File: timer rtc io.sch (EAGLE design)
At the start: 71 parts, among them T1 BC547, U1 74HC245, U10 74HC688, U11 74LS30N, U12 74LS00N, U13 74HC32, U14 74HC04, U15 74HC08, U16 74HC688, U17 74HC138, U18 74HC138, U19 74HC573, U2 74HC245, U20 74HC573, U21 74HC573, U22 74HC573, U23 74HC573, U3 74HC245, U4 74HC688, U6 74HC74, U7 74HC590, U8 74HC688, U9 BQ4845, X1 32.768KHz, Y1 4.096MHz

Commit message: A few changes:
* renamed source files to .s
* moved some stuff to .inc files
* a couple of HW updates to some boars to provide a bigger RAM space for UART loading
* SIO module for serial comms
* serial loader code to work with the above
* scripts for loading/reading/executing via serial

I think thats it...
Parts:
- added C26, C27, C28: 100nF, rcl:C-EU050-025X075
- added R3: 10K, rcl:R-EU_0207/10
- added R4, R5: 560R, rcl:R-EU_0207/10
- added U24: NE555, st-microelectronics:NE555
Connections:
- removed net N$48: U11A.I6, U17A.Y3, U22A.C, U22A.OC
- new net N$53: BUS-15.S, R3.1, U5.IEI
- new net N$60: R1.1, SG1.2, U24.OUT
- new net N$88: R4.1, R5.2, U24.DIS
- new net N$89: C28.1, R5.1, U24.TRE, U24.TRI
- new net N$90: U11A.I6, U17A.Y3, U21A.C, U21A.OC
- net +5V: now also C26.1, R3.2, R4.2, U24.VCC+; no longer U5.IEI
- net GND: now also C26.2, C27.2, C28.2, U24.GND
- net N$47: now also U22A.C, U22A.OC; no longer U21A.C, U21A.OC
- net N$55: now also C27.1, U24.CON; no longer R2.1, U23A.8Q
- net N$56: now also U23A.8Q, U24./RES; no longer R1.1, SG1.2, T1.C
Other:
- note added: "BUTTONS 08"
- note added: "OUTPUTS 0C"
- note added: "R4=560R R5=560R ~66% D/C ~8.6KHZ R4=1K5 R5=150R ~91% D/C ~8KHZ"
- note added: "SWITCHES 1 09"
- note added: "SWITCHES 2 0A"
- note added: "SWITCHES 3 0B"
- moved on the sheet: BUS-15, C10, C11, C12, C13, C14, C15, C16, C17, C18, C19, C2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

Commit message: Discovered issue with Timer/RTC/IO board
The original design of the Timer/RTC/IO board did not cater for a situation where multiple Z80 peripherals may exist in the system.

Consequently, when M1/ and IORQ/ are both asserted by the CPU to read a vector from the interrupting peripheral, and if that peripheral happens to be the SIO, the Timer/RTC/IO board will configure its data bus buffer for output towards the CPU. If the SIO is responding with its vector, this causes contention on that portion of the bus, resulting in interupts to random vectors.

Staged some logic for a subsequent modification (gates U14B and U13A) which would prevent the Timer/RTC/IO board from configuring its data bus buffer outwards if the IEI/ signal is asserted. However, this logic isnt latched in any way, so it could be interrupted half way through if IEI/ is asserted while outputting a vector... Perhaps more thought needed.
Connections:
- new net !IEI!: BUS-15.S, R3.1, U14B.I, U5.IEI
- new net N$48: U13A.O
- net GND: no longer U13A.I0, U13A.I1, U14B.I
- net N$53: now also U13A.I0, U14B.O; no longer BUS-15.S, R3.1, U5.IEI
- net N$61: now also U13A.I1
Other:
- moved on the sheet: BAT1, BUS-15, JP1, R3, RN2-1, RN2-2, RN2-3, RN2-4, RN2_, U10, U13A, U14A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

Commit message: Interrupt daisy chain modification
To overcome the issue identified earlier, it seems better to change the interrupt daisy chain to make the CTC the higher priority device. This also simplifies the extra required circuitry to only a single OR gate (U13A).

Now, only when the IEO/ signal of the CTC is asserted will the board drive the data bus to the CPU.

Also added in a previous revision is changes to the beeper circuit. Will now be driven by a 555 timer, gated by the output register.
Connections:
- removed net !IEI!: BUS-15.S, R3.1, U14B.I, U5.IEI
- removed net N$53: U13A.I0, U14B.O
- new net !IEO!: BUS-15.S, U13A.I0, U5.IEO
- net +5V: now also U5.IEI; no longer R3.2
- net GND: now also U14B.I
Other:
- moved on the sheet: BUS-15, R3, U11, U12A, U13A, U13C, U14B, U14F, U15A

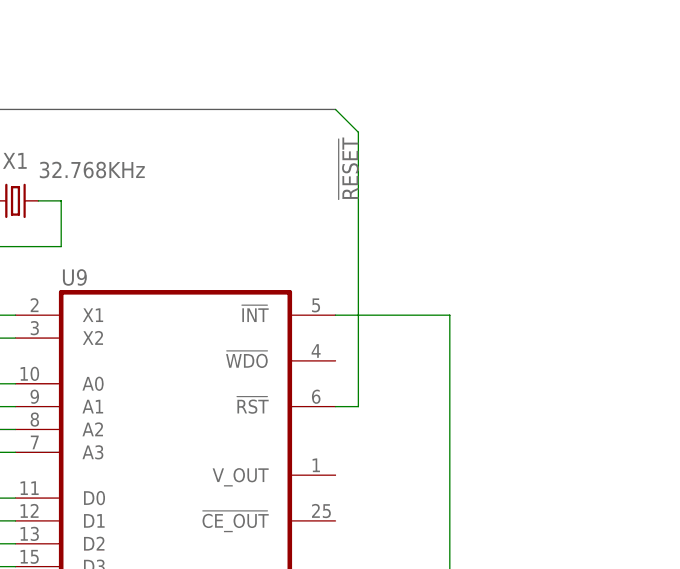
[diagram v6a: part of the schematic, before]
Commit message: Add jumper to output of RST/ pin on RTC
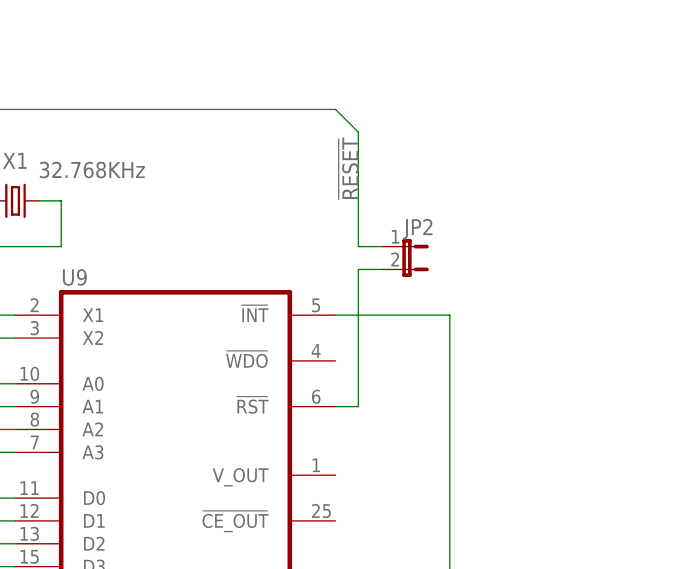
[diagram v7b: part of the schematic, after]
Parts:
- added JP2: (no value), jumper:JP1E
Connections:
- new net N$53: JP2.2, U9.!RST!
- net !RESET!: now also JP2.1; no longer U9.!RST!
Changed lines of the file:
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@@
 <part name="C28" library="rcl" deviceset="C-EU" device="050-025X075" value="100nF"/>
 <part name="GND32" library="supply1" deviceset="GND" device=""/>
+<part name="JP2" library="jumper" deviceset="JP1E" device=""/>
 </parts>
 <sheets>
@@
 <attribute name="VALUE" x="228.6" y="-127" size="1.778" layer="96"/>
 </instance>
+<instance part="JP2" gate="A" x="535.94" y="147.32" smashed="yes" rot="R270">
+<attribute name="NAME" x="535.94" y="148.59" size="1.778" layer="95"/>
+<attribute name="VALUE" x="535.94" y="141.605" size="1.778" layer="96"/>
+</instance>
 </instances>
 <busses>
@@
 <segment>
 <wire x1="528.32" y1="162.56" x2="530.86" y2="160.02" width="0.1524" layer="91"/>
-<wire x1="530.86" y1="160.02" x2="530.86" y2="129.54" width="0.1524" layer="91"/>
-<pinref part="U9" gate="G$1" pin="!RST!"/>
-<wire x1="530.86" y1="129.54" x2="528.32" y2="129.54" width="0.1524" layer="91"/>
+<wire x1="530.86" y1="160.02" x2="530.86" y2="147.32" width="0.1524" layer="91"/>
+<pinref part="JP2" gate="A" pin="1"/>
+<wire x1="533.4" y1="147.32" x2="530.86" y2="147.32" width="0.1524" layer="91"/>
 <label x="530.86" y="152.4" size="1.778" layer="95" rot="R90"/>
 </segment>
@@
 </segment>
 </net>
+<net name="N$53" class="0">
+<segment>
+<pinref part="U9" gate="G$1" pin="!RST!"/>
+<wire x1="530.86" y1="144.78" x2="530.86" y2="129.54" width="0.1524" layer="91"/>
+<wire x1="530.86" y1="129.54" x2="528.32" y2="129.54" width="0.1524" layer="91"/>
+<pinref part="JP2" gate="A" pin="2"/>
+<wire x1="533.4" y1="144.78" x2="530.86" y2="144.78" width="0.1524" layer="91"/>
+</segment>
+</net>

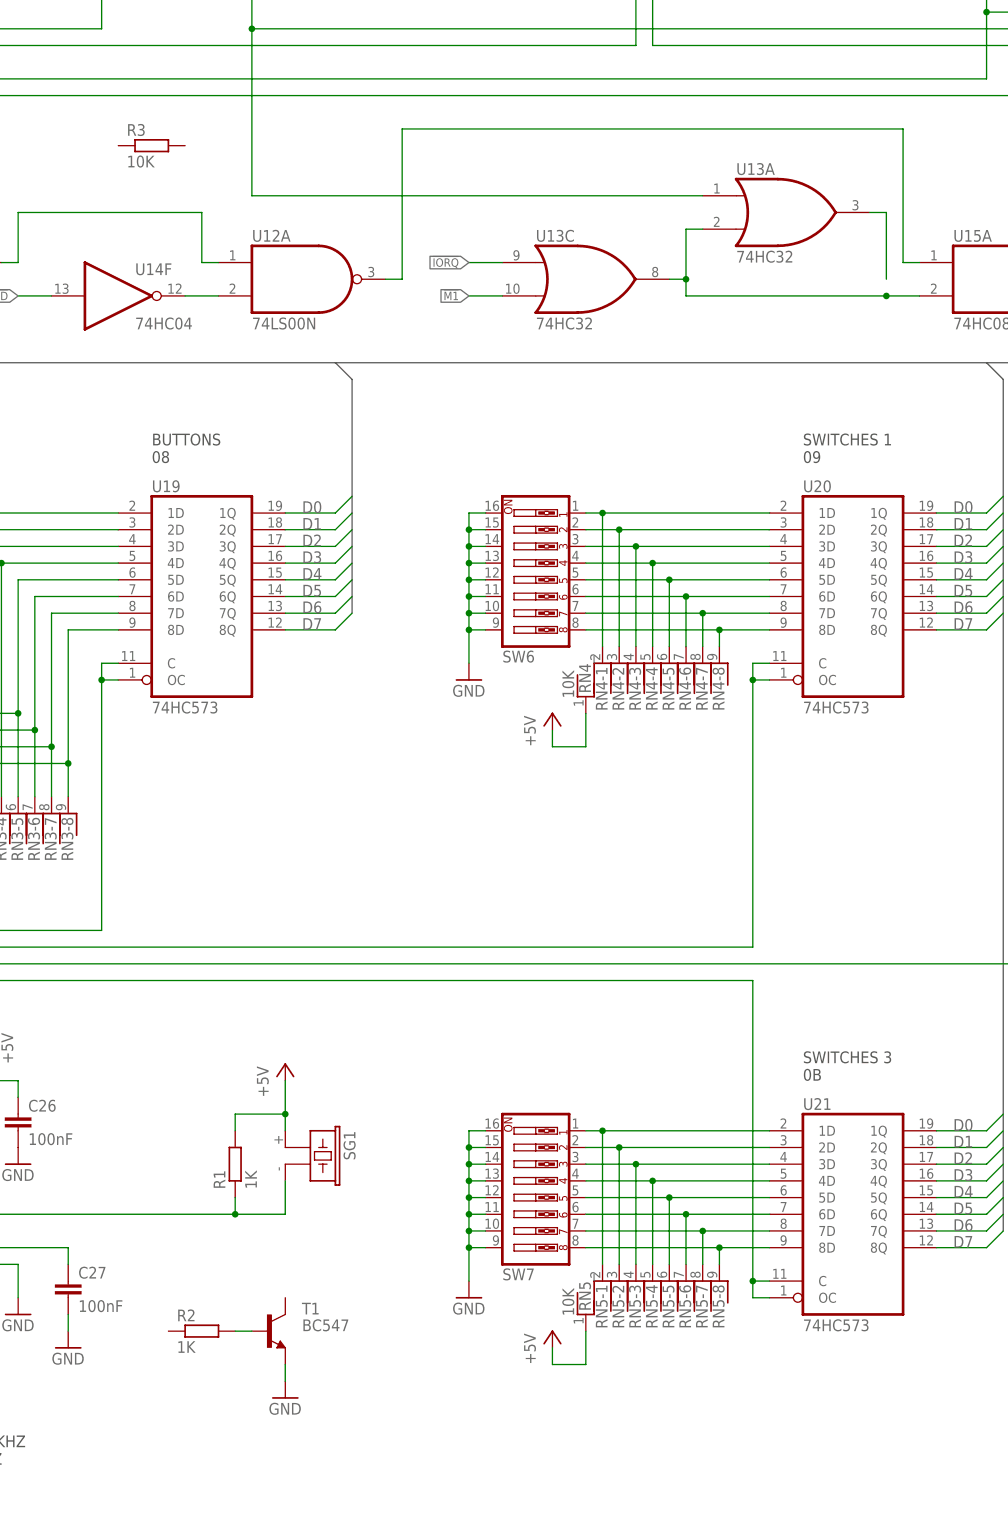
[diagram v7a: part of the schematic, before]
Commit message: Correct schematic for new interrupt daisy chain priority
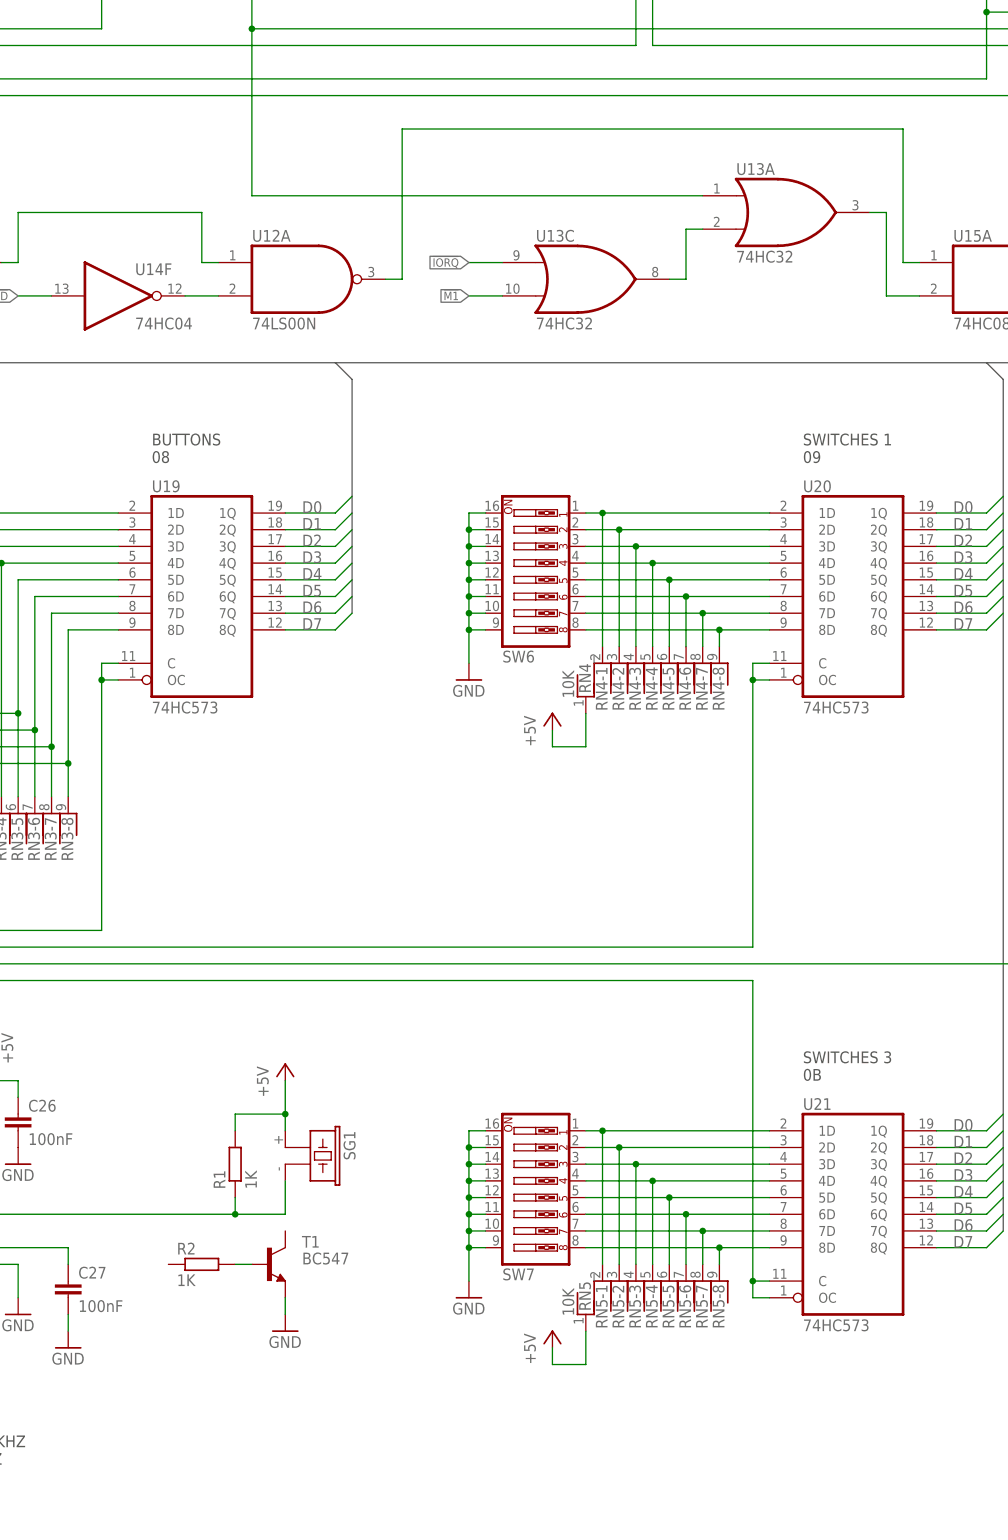
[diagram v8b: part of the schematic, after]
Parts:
- removed R3: 10K, rcl:R-EU_0207/10
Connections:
- removed net N$61: U13A.I1, U13C.O, U15A.I1
- new net N$91: U13A.I1, U13C.O
- net N$48: now also U15A.I1
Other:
- moved on the sheet: R2, T1
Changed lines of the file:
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@@
 <part name="GND28" library="supply1" deviceset="GND" device=""/>
 <part name="C25" library="rcl" deviceset="C-EU" device="050-025X075" value="100nF"/>
-<part name="R3" library="rcl" deviceset="R-EU_" device="0207/10" value="10K"/>
 <part name="U24" library="st-microelectronics" deviceset="NE555" device=""/>
 <part name="P+23" library="supply1" deviceset="+5V" device=""/>
@@
 <text x="195.58" y="-76.2" size="1.778" layer="97">OUTPUTS
 0C</text>
-<wire x1="223.52" y1="-68.58" x2="327.66" y2="-68.58" width="0.6096" layer="90"/>
-<wire x1="327.66" y1="-68.58" x2="327.66" y2="-144.78" width="0.6096" layer="90"/>
+<wire x1="223.52" y1="-71.12" x2="327.66" y2="-71.12" width="0.6096" layer="90"/>
+<wire x1="327.66" y1="-71.12" x2="327.66" y2="-144.78" width="0.6096" layer="90"/>
 <wire x1="327.66" y1="-144.78" x2="223.52" y2="-144.78" width="0.6096" layer="90"/>
-<wire x1="223.52" y1="-144.78" x2="223.52" y2="-68.58" width="0.6096" layer="90"/>
+<wire x1="223.52" y1="-144.78" x2="223.52" y2="-71.12" width="0.6096" layer="90"/>
 <text x="228.6" y="-139.7" size="1.778" layer="97">R4=560R R5=560R ~66% D/C ~8.6KHZ
 R4=1K5 R5=150R ~91% D/C ~8KHZ</text>
-<wire x1="363.22" y1="63.5" x2="447.04" y2="63.5" width="0.6096" layer="90"/>
-<wire x1="447.04" y1="63.5" x2="447.04" y2="33.02" width="0.6096" layer="90"/>
-<wire x1="447.04" y1="33.02" x2="363.22" y2="33.02" width="0.6096" layer="90"/>
-<wire x1="363.22" y1="33.02" x2="363.22" y2="63.5" width="0.6096" layer="90"/>
 </plain>
 <instances>
@@
 <attribute name="VALUE" x="314.96" y="-97.79" size="1.778" layer="96" rot="R270"/>
 </instance>
-<instance part="GND17" gate="1" x="312.42" y="-129.54" smashed="yes">
-<attribute name="VALUE" x="309.88" y="-132.08" size="1.778" layer="96"/>
+<instance part="GND17" gate="1" x="312.42" y="-119.38" smashed="yes">
+<attribute name="VALUE" x="309.88" y="-121.92" size="1.778" layer="96"/>
 </instance>
 <instance part="P+13" gate="1" x="312.42" y="-78.74" smashed="yes">
@@
 <attribute name="VALUE" x="27.94" y="-60.96" size="1.778" layer="96"/>
 </instance>
-<instance part="T1" gate="G$1" x="309.88" y="-119.38" smashed="yes">
-<attribute name="NAME" x="314.96" y="-116.84" size="1.778" layer="95"/>
-<attribute name="VALUE" x="314.96" y="-119.38" size="1.778" layer="96"/>
-</instance>
-<instance part="R2" gate="G$1" x="299.72" y="-119.38" smashed="yes">
-<attribute name="NAME" x="295.91" y="-117.8814" size="1.778" layer="95"/>
-<attribute name="VALUE" x="295.91" y="-122.682" size="1.778" layer="96"/>
+<instance part="T1" gate="G$1" x="309.88" y="-109.22" smashed="yes">
+<attribute name="NAME" x="314.96" y="-106.68" size="1.778" layer="95"/>
+<attribute name="VALUE" x="314.96" y="-109.22" size="1.778" layer="96"/>
+</instance>
+<instance part="R2" gate="G$1" x="299.72" y="-109.22" smashed="yes">
+<attribute name="NAME" x="295.91" y="-107.7214" size="1.778" layer="95"/>
+<attribute name="VALUE" x="295.91" y="-112.522" size="1.778" layer="96"/>
 </instance>
 <instance part="U11" gate="A" x="256.54" y="43.18" smashed="yes">
@@
 <attribute name="VALUE" x="481.584" y="-197.739" size="1.778" layer="96"/>
 </instance>
-<instance part="R3" gate="G$1" x="292.1" y="60.96" smashed="yes">
-<attribute name="NAME" x="288.29" y="62.4586" size="1.778" layer="95"/>
-<attribute name="VALUE" x="288.29" y="57.658" size="1.778" layer="96"/>
-</instance>
 <instance part="U24" gate="G$1" x="251.46" y="-101.6" smashed="yes">
 <attribute name="NAME" x="243.84" y="-90.17" size="1.778" layer="95"/>
@@
 <segment>
 <pinref part="GND17" gate="1" pin="GND"/>
-<wire x1="312.42" y1="-127" x2="312.42" y2="-124.46" width="0.1524" layer="91"/>
+<wire x1="312.42" y1="-116.84" x2="312.42" y2="-114.3" width="0.1524" layer="91"/>
 <pinref part="T1" gate="G$1" pin="E"/>
 </segment>
@@
 <pinref part="T1" gate="G$1" pin="B"/>
 <pinref part="R2" gate="G$1" pin="2"/>
-<wire x1="307.34" y1="-119.38" x2="304.8" y2="-119.38" width="0.1524" layer="91"/>
+<wire x1="307.34" y1="-109.22" x2="304.8" y2="-109.22" width="0.1524" layer="91"/>
 </segment>
 </net>
@@
 </segment>
 </net>
-<net name="N$61" class="0">
-<segment>
-<pinref part="U13" gate="C" pin="O"/>
-<wire x1="370.84" y1="40.64" x2="373.38" y2="40.64" width="0.1524" layer="91"/>
-<wire x1="373.38" y1="40.64" x2="373.38" y2="38.1" width="0.1524" layer="91"/>
-<pinref part="U15" gate="A" pin="I1"/>
-<wire x1="373.38" y1="38.1" x2="403.86" y2="38.1" width="0.1524" layer="91"/>
-<pinref part="U13" gate="A" pin="I1"/>
-<wire x1="403.86" y1="38.1" x2="408.94" y2="38.1" width="0.1524" layer="91"/>
-<wire x1="375.92" y1="48.26" x2="373.38" y2="48.26" width="0.1524" layer="91"/>
-<wire x1="373.38" y1="48.26" x2="373.38" y2="40.64" width="0.1524" layer="91"/>
-<junction x="373.38" y="40.64"/>
-<junction x="403.86" y="38.1"/>
-</segment>
-</net>
 <net name="N$87" class="0">
 <segment>
@@
 <pinref part="U13" gate="A" pin="O"/>
 <wire x1="401.32" y1="50.8" x2="403.86" y2="50.8" width="0.1524" layer="91"/>
-<wire x1="403.86" y1="50.8" x2="403.86" y2="40.64" width="0.1524" layer="91"/>
+<wire x1="403.86" y1="50.8" x2="403.86" y2="38.1" width="0.1524" layer="91"/>
+<pinref part="U15" gate="A" pin="I1"/>
+<wire x1="403.86" y1="38.1" x2="408.94" y2="38.1" width="0.1524" layer="91"/>
 </segment>
 </net>
@@
 </segment>
 </net>
+<net name="N$91" class="0">
+<segment>
+<pinref part="U13" gate="A" pin="I1"/>
+<wire x1="375.92" y1="48.26" x2="373.38" y2="48.26" width="0.1524" layer="91"/>
+<wire x1="373.38" y1="48.26" x2="373.38" y2="40.64" width="0.1524" layer="91"/>
+<pinref part="U13" gate="C" pin="O"/>
+<wire x1="370.84" y1="40.64" x2="373.38" y2="40.64" width="0.1524" layer="91"/>
+</segment>
+</net>
